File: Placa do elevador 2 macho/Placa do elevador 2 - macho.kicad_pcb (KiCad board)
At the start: 2 copper layers, 7 parts, among them J1 DB25_Male, J2 Conn_01x04, J3 Conn_01x04, J4 Conn_01x04, J5 Conn_01x04, J6 Conn_01x04, J7 Conn_01x04

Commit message: Mudando de nome e atualizando os perfis
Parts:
- moved J3 5.14 mm to (190.2, 82.5)
- moved J2 5.14 mm to (113.5, 72.1)
- moved J6 5.14 mm to (140.7, 81.3)
- moved J7 5.14 mm to (153.4, 81.3)
- moved J1 5.14 mm to (168.5, 61.5)
- moved J5 5.14 mm to (192.3, 50.3)
- moved J4 5.14 mm to (170.6, 81.5)
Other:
- board outline added: 102.6 x 70.1 mm

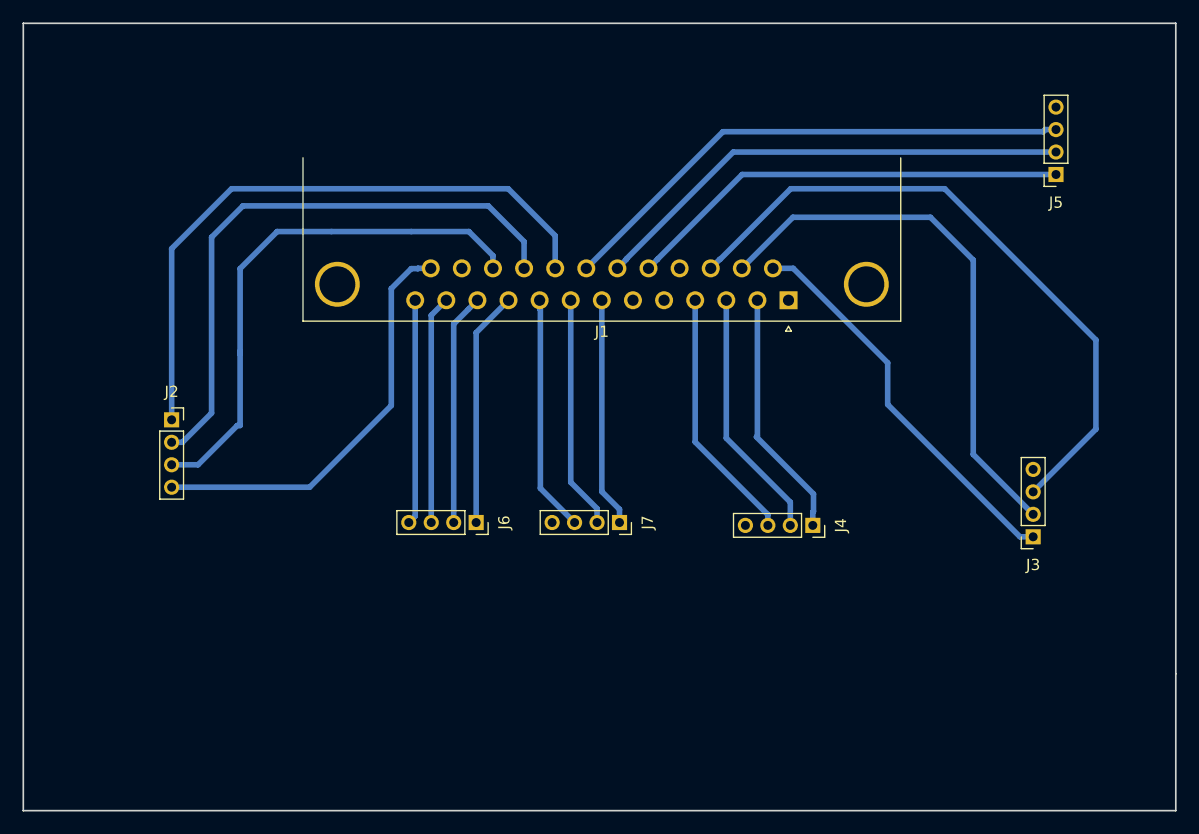
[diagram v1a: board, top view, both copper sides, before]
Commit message: Adicionando parafusos
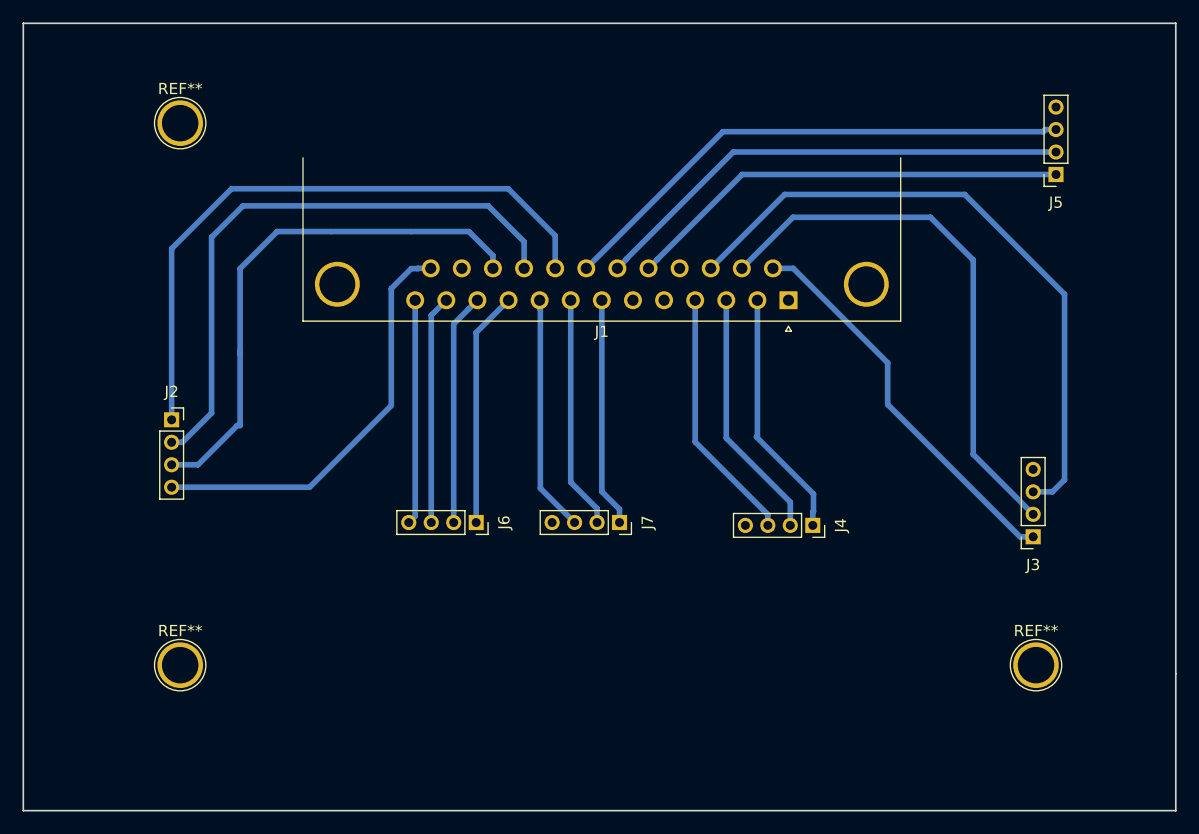
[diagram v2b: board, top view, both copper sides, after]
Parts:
- added REF**: 1pin, Connectors:1pin, F.Cu at (114.3, 45.7)
- added REF**: 1pin, Connectors:1pin, F.Cu at (114.3, 94.0)
- added REF**: 1pin, Connectors:1pin, F.Cu at (190.5, 94.0)
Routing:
- net B5: track 58.6 -> 57.7 mm
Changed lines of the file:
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@@
-(kicad_pcb (version 20171130) (host pcbnew 5.0.1-33cea8e~68~ubuntu16.04.1)
+(kicad_pcb (version 20171130) (host pcbnew "(5.0.0)")
   (general
     (thickness 1.6)
-    (drawings 6)
-    (tracks 91)
+    (drawings 7)
+    (tracks 90)
     (zones 0)
-    (modules 7)
+    (modules 10)
     (nets 30)
   )
@@
     (mod_text_size 1 1)
     (mod_text_width 0.15)
-    (pad_size 1.524 1.524)
-    (pad_drill 0.762)
+    (pad_size 4.064 4.064)
+    (pad_drill 3.248)
     (pad_to_mask_clearance 0.2)
     (solder_mask_min_width 0.25)
     (aux_axis_origin 0 0)
-    (visible_elements FFFFFF7F)
+    (visible_elements 7FFFFFFF)
     (pcbplotparams
       (layerselection 0x010fc_ffffffff)
@@
     (uvia_drill 0.1)
   )
+  (module Connectors:1pin (layer F.Cu)
+    (at 114.3 45.72)
+    (descr "module 1 pin (ou trou mecanique de percage)")
+    (tags DEV)
+    (fp_text reference REF** (at 0 -3.048) (layer F.SilkS)
+      (effects (font (size 1 1) (thickness 0.15)))
+    )
+    (fp_text value 1pin (at 0 3) (layer F.Fab)
+      (effects (font (size 1 1) (thickness 0.15)))
+    )
+    (fp_circle (center 0 0) (end 2 0.8) (layer F.Fab) (width 0.1))
+    (fp_circle (center 0 0) (end 2.6 0) (layer F.CrtYd) (width 0.05))
+    (fp_circle (center 0 0) (end 0 -2.286) (layer F.SilkS) (width 0.12))
+    (pad 1 thru_hole circle (at 0 0) (size 4.064 4.064) (drill 3.248) (layers *.Cu *.Mask))
+  )
+  (module Connectors:1pin (layer F.Cu)
+    (at 114.3 93.98)
+    (descr "module 1 pin (ou trou mecanique de percage)")
+    (tags DEV)
+    (fp_text reference REF** (at 0 -3.048) (layer F.SilkS)
+      (effects (font (size 1 1) (thickness 0.15)))
+    )
+    (fp_text value 1pin (at 0 3) (layer F.Fab)
+      (effects (font (size 1 1) (thickness 0.15)))
+    )
+    (fp_circle (center 0 0) (end 0 -2.286) (layer F.SilkS) (width 0.12))
+    (fp_circle (center 0 0) (end 2.6 0) (layer F.CrtYd) (width 0.05))
+    (fp_circle (center 0 0) (end 2 0.8) (layer F.Fab) (width 0.1))
+    (pad 1 thru_hole circle (at 0 0) (size 4.064 4.064) (drill 3.248) (layers *.Cu *.Mask))
+  )
   (module Connector_Dsub:DSUB-25_Male_Horizontal_P2.77x2.84mm_EdgePinOffset9.90mm_Housed_MountingHolesOffset11.32mm (layer F.Cu)
     (at 168.463001 61.488339 180)
@@
     )
   )
-  (dimension 7.62 (width 0.3) (layer Dwgs.User)
-    (gr_text "7,620 mm" (at 214.19 45.72 270) (layer Dwgs.User)
+  (module Connectors:1pin (layer F.Cu)
+    (at 190.5 93.98)
+    (descr "module 1 pin (ou trou mecanique de percage)")
+    (tags DEV)
+    (fp_text reference REF** (at 0 -3.048) (layer F.SilkS)
+      (effects (font (size 1 1) (thickness 0.15)))
+    )
+    (fp_text value 1pin (at 0 3) (layer F.Fab)
+      (effects (font (size 1 1) (thickness 0.15)))
+    )
+    (fp_circle (center 0 0) (end 2 0.8) (layer F.Fab) (width 0.1))
+    (fp_circle (center 0 0) (end 2.6 0) (layer F.CrtYd) (width 0.05))
+    (fp_circle (center 0 0) (end 0 -2.286) (layer F.SilkS) (width 0.12))
+    (pad 1 thru_hole circle (at 0 0) (size 4.064 4.064) (drill 3.248) (layers *.Cu *.Mask))
+  )
+  (dimension 70.104 (width 0.3) (layer B.SilkS)
+    (gr_text "70.104 mm" (at 213.428 71.882 270) (layer B.SilkS)
       (effects (font (size 1.5 1.5) (thickness 0.3)))
     )
-    (feature1 (pts (xy 188.468 49.53) (xy 212.676421 49.53)))
-    (feature2 (pts (xy 188.468 41.91) (xy 212.676421 41.91)))
-    (crossbar (pts (xy 212.09 41.91) (xy 212.09 49.53)))
-    (arrow1a (pts (xy 212.09 49.53) (xy 211.503579 48.403496)))
-    (arrow1b (pts (xy 212.09 49.53) (xy 212.676421 48.403496)))
-    (arrow2a (pts (xy 212.09 41.91) (xy 211.503579 43.036504)))
-    (arrow2b (pts (xy 212.09 41.91) (xy 212.676421 43.036504)))
+    (feature1 (pts (xy 202.946 106.934) (xy 211.914421 106.934)))
+    (feature2 (pts (xy 202.946 36.83) (xy 211.914421 36.83)))
+    (crossbar (pts (xy 211.328 36.83) (xy 211.328 106.934)))
+    (arrow1a (pts (xy 211.328 106.934) (xy 210.741579 105.807496)))
+    (arrow1b (pts (xy 211.328 106.934) (xy 211.914421 105.807496)))
+    (arrow2a (pts (xy 211.328 36.83) (xy 210.741579 37.956504)))
+    (arrow2b (pts (xy 211.328 36.83) (xy 211.914421 37.956504)))
+  )
+  (dimension 102.616 (width 0.3) (layer B.SilkS)
+    (gr_text "102.616 mm" (at 151.638 120.464) (layer B.SilkS)
+      (effects (font (size 1.5 1.5) (thickness 0.3)))
+    )
+    (feature1 (pts (xy 202.946 106.934) (xy 202.946 118.950421)))
+    (feature2 (pts (xy 100.33 106.934) (xy 100.33 118.950421)))
+    (crossbar (pts (xy 100.33 118.364) (xy 202.946 118.364)))
+    (arrow1a (pts (xy 202.946 118.364) (xy 201.819496 118.950421)))
+    (arrow1b (pts (xy 202.946 118.364) (xy 201.819496 117.777579)))
+    (arrow2a (pts (xy 100.33 118.364) (xy 101.456504 118.950421)))
+    (arrow2b (pts (xy 100.33 118.364) (xy 101.456504 117.777579)))
   )
   (gr_line (start 100.33 106.934) (end 202.946 106.934) (layer Edge.Cuts) (width 0.15))
@@
   (segment (start 168.85434 54.102) (end 164.308001 58.648339) (width 0.5) (layer B.Cu) (net 19))
   (segment (start 181.102 54.102) (end 168.85434 54.102) (width 0.5) (layer B.Cu) (net 19))
-  (segment (start 162.338 57.84834) (end 162.36966 57.84834) (width 0.5) (layer B.Cu) (net 20))
-  (segment (start 161.538001 58.648339) (end 162.338 57.84834) (width 0.5) (layer B.Cu) (net 20))
-  (segment (start 162.36966 57.84834) (end 168.656 51.562) (width 0.5) (layer B.Cu) (net 20))
-  (segment (start 168.656 51.562) (end 182.372 51.562) (width 0.5) (layer B.Cu) (net 20))
-  (segment (start 182.372 51.562) (end 195.834 65.024) (width 0.5) (layer B.Cu) (net 20))
-  (segment (start 195.834 72.962) (end 190.246 78.55) (width 0.5) (layer B.Cu) (net 20))
-  (segment (start 195.834 65.024) (end 195.834 72.962) (width 0.5) (layer B.Cu) (net 20))
-  (segment (start 156.798 57.84834) (end 156.798 57.832) (width 0.5) (layer B.Cu) (net 21))
+  (segment (start 190.246 78.55) (end 191.96 78.55) (width 0.5) (layer B.Cu) (net 20) (status 400000))
+  (segment (start 168.11634 52.07) (end 161.538001 58.648339) (width 0.5) (layer B.Cu) (net 20) (status 800000))
+  (segment (start 184.15 52.07) (end 168.11634 52.07) (width 0.5) (layer B.Cu) (net 20))
+  (segment (start 193.04 60.96) (end 184.15 52.07) (width 0.5) (layer B.Cu) (net 20))
+  (segment (start 193.04 77.47) (end 193.04 60.96) (width 0.5) (layer B.Cu) (net 20))
+  (segment (start 191.96 78.55) (end 193.04 77.47) (width 0.5) (layer B.Cu) (net 20))
   (segment (start 155.998001 58.648339) (end 156.798 57.84834) (width 0.5) (layer B.Cu) (net 21))
   (segment (start 164.338 50.292) (end 192.278 50.292) (width 0.5) (layer B.Cu) (net 21))
   (segment (start 156.798 57.832) (end 164.338 50.292) (width 0.5) (layer B.Cu) (net 21))
-  (segment (start 154.028 57.84834) (end 154.028 57.808) (width 0.5) (layer B.Cu) (net 22))
+  (segment (start 156.798 57.84834) (end 156.798 57.832) (width 0.5) (layer B.Cu) (net 21))
   (segment (start 153.228001 58.648339) (end 154.028 57.84834) (width 0.5) (layer B.Cu) (net 22))
   (segment (start 163.544 48.292) (end 192.278 48.292) (width 0.5) (layer B.Cu) (net 22))
   (segment (start 154.028 57.808) (end 163.544 48.292) (width 0.5) (layer B.Cu) (net 22))
-  (segment (start 191.323406 46.292) (end 191.133406 46.482) (width 0.5) (layer B.Cu) (net 23))
+  (segment (start 154.028 57.84834) (end 154.028 57.808) (width 0.5) (layer B.Cu) (net 22))
   (segment (start 192.278 46.292) (end 191.323406 46.292) (width 0.5) (layer B.Cu) (net 23))
   (segment (start 162.62434 46.482) (end 150.458001 58.648339) (width 0.5) (layer B.Cu) (net 23))
   (segment (start 191.133406 46.482) (end 162.62434 46.482) (width 0.5) (layer B.Cu) (net 23))
+  (segment (start 191.323406 46.292) (end 191.133406 46.482) (width 0.5) (layer B.Cu) (net 23))
   (segment (start 147.688001 55.740001) (end 147.688001 58.648339) (width 0.5) (layer B.Cu) (net 24))
   (segment (start 113.538 56.896) (end 118.872 51.562) (width 0.5) (layer B.Cu) (net 24))
